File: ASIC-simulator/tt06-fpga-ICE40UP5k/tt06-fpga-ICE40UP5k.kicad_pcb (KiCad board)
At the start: 4 copper layers, 50 x 53 mm, 116 parts, among them CON1 NPTC202KFMS-RC, CON2 NPTC202KFMS-RC, U1 ICE40UP5K-SG48I, U2 AP2112K-1.2, X1 24MHz

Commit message: minor pcb touch-ups
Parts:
- added STITCH01: StitchingVia-0.4mmDrill, flyingcarsfootprints:StitchingVia-0.4mmDrill, F.Cu at (59.4, 29.0)
- moved STITCH01 0.92 mm to (63.4, 29.0)
- moved STITCH01 0.10 mm to (75.3, 56.9)

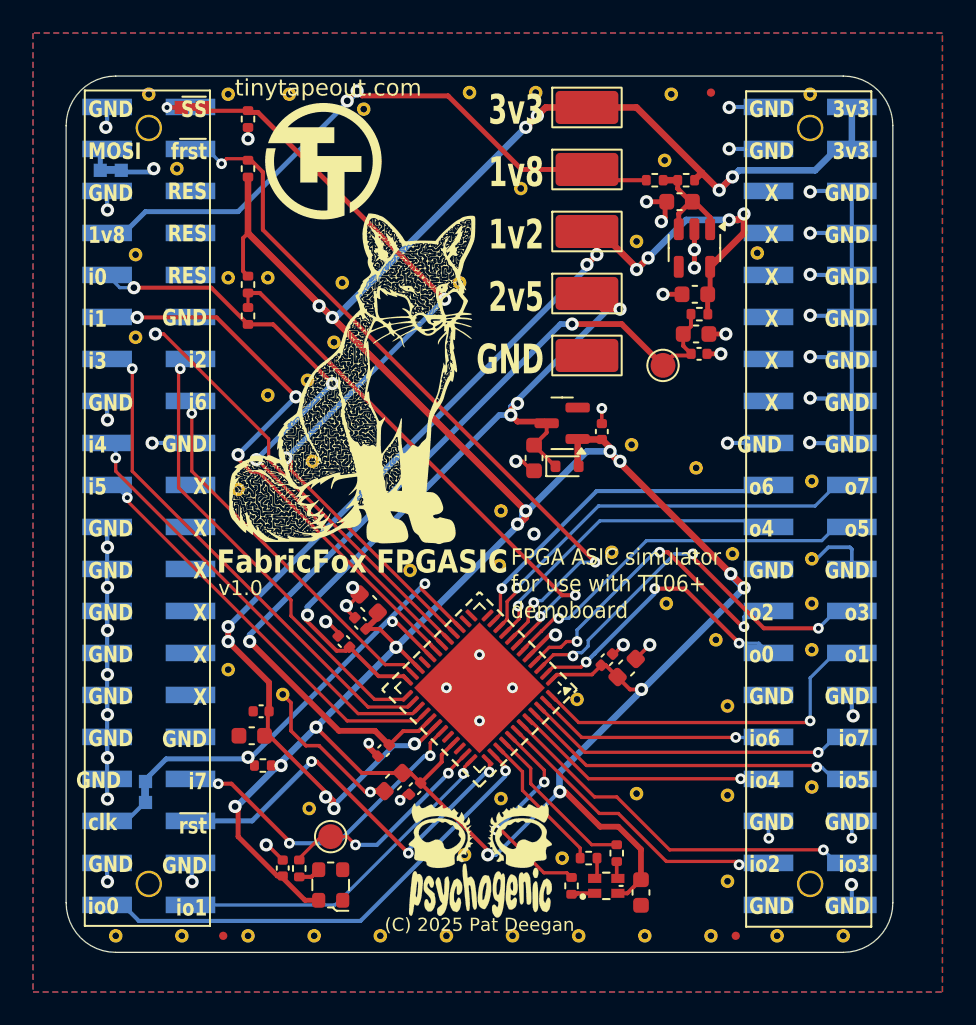
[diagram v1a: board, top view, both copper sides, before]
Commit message: LCSC components and minor layout tweaks for production run
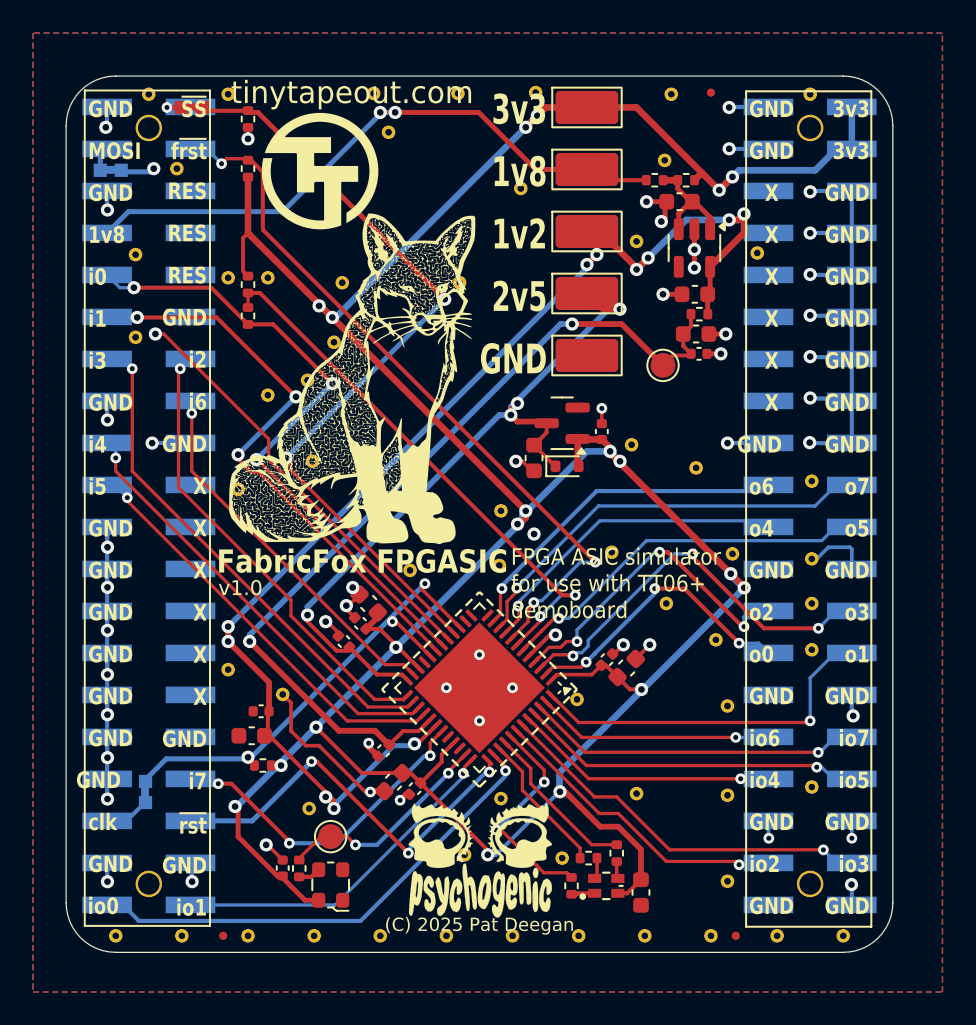
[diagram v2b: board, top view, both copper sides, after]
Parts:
- moved STITCH01 5.10 mm to (53.6, 29.1)
- moved STITCH01 2.05 mm to (54.5, 31.4)
- moved STITCH01 0.70 mm to (58.7, 29.1)
- moved TTLOGO1 0.63 mm to (50.4, 33.8)
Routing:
- net +1V8: track 39.3 -> 38.2 mm

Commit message: v1.1 CDONE LED
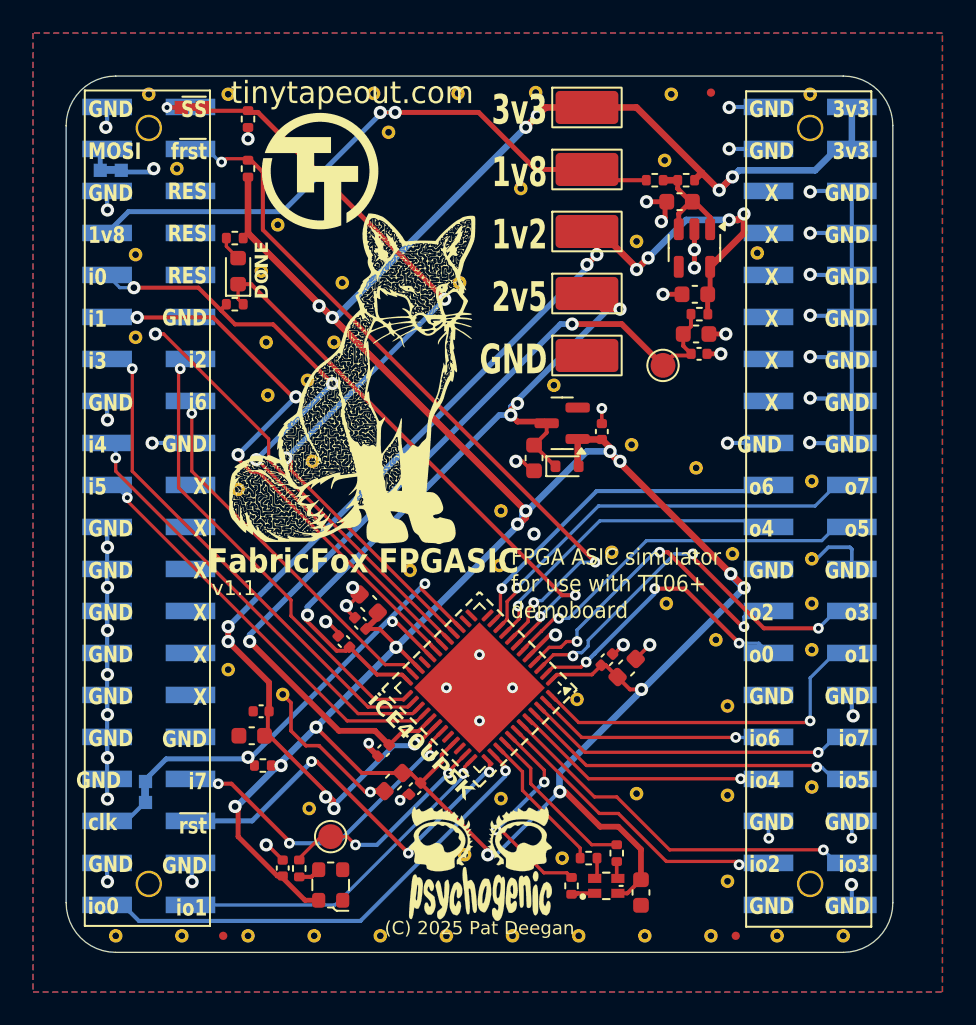
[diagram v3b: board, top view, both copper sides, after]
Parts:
- added D4: LED, LED_SMD:LED_0603_1608Metric, F.Cu at (45.4, 39.8)
- added STITCH01: StitchingVia-0.4mmDrill, flyingcarsfootprints:StitchingVia-0.4mmDrill, F.Cu at (64.5, 46.7)
- added STITCH01: StitchingVia-0.4mmDrill, flyingcarsfootprints:StitchingVia-0.4mmDrill, F.Cu at (46.8, 39.8)
- R1: value 1k -> 10k
- R10: value 10k -> 100
- moved STITCH01 4.53 mm to (47.1, 44.1)
- moved STITCH01 3.26 mm to (47.8, 37.0)
- moved R10 2.92 mm to (45.2, 37.8), turned to 0 degrees
- moved R1 1.07 mm to (45.2, 41.8), turned to 180 degrees
- moved {$REFERENCE} 0.20 mm to (60.0, 75.6)
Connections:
- R10 pad 1: +3V3 -> Net-(D4-A)
- R10 pad 2: /FPGA/CDONE -> +3V3
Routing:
- net +3V3: track 197.8 -> 195.4 mm
- net Net-(D4-A): track 0.00 -> 1.51 mm
- net /FPGA/CDONE: track 33.2 -> 34.5 mm
- net /uin0: track 38.8 -> 39.3 mm
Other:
- board text added: "DONE"
- board text added: "iCE40UP5K"
- board text added: "v${REVISION}"
- board text removed: "v1.0"
